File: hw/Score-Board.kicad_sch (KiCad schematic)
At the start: 95 parts, among them J1 Barrel_Jack, J2 Screw_Terminal_01x02, J3 Conn_01x04, J4 Conn_01x03, J5 Conn_01x04, J6 J-V3.3, J7 J-V12, J8 J-VSYS, Q1 2N3904, Q10 2N3905, Q11 2N3905, Q12 2N3905, Q13 2N3905, Q14 2N3905, Q15 2N3904, Q16 2N3904, Q17 2N3904, Q18 2N3904, Q19 2N3904, Q2 2N3904, Q20 2N3904, Q21 2N3904, Q22 2N3904, Q3 2N3904, Q4 2N3904, Q5 2N3904, Q6 2N3904, Q7 2N3904, Q8 2N3905, Q9 2N3905, SW1 RESET, SW2 NETWORK, U1 PicoW, U2 E18-MS1-PCB, U5 MCP1702-5002E

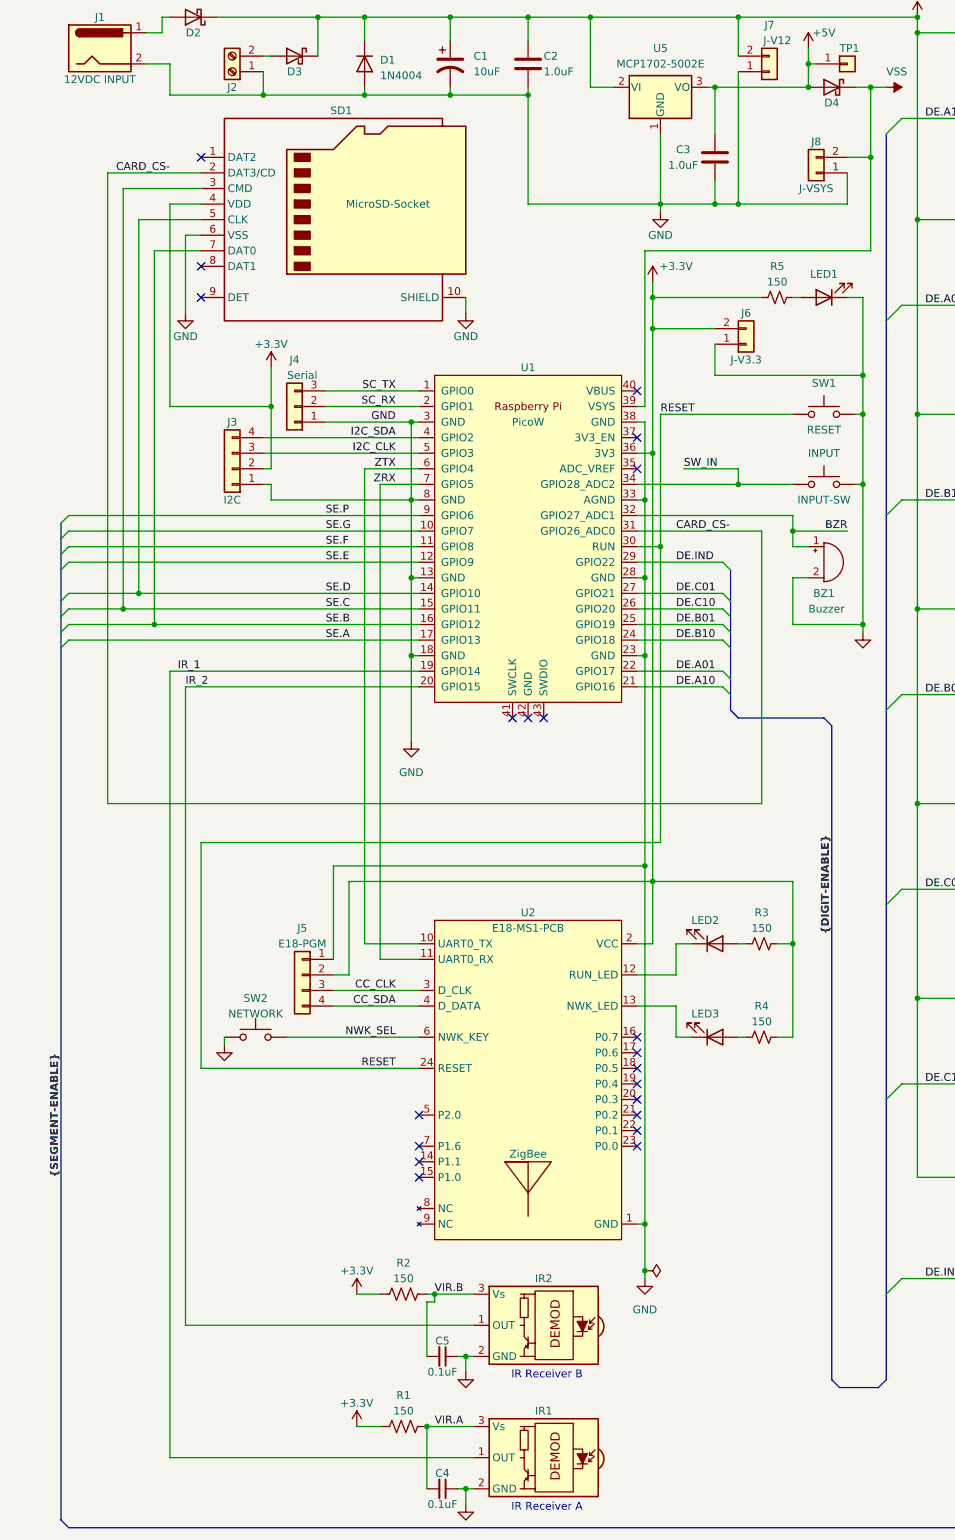
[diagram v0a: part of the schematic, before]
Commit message: SPI for display & SD, Seg&Dig enables 16 straight GPIOs.
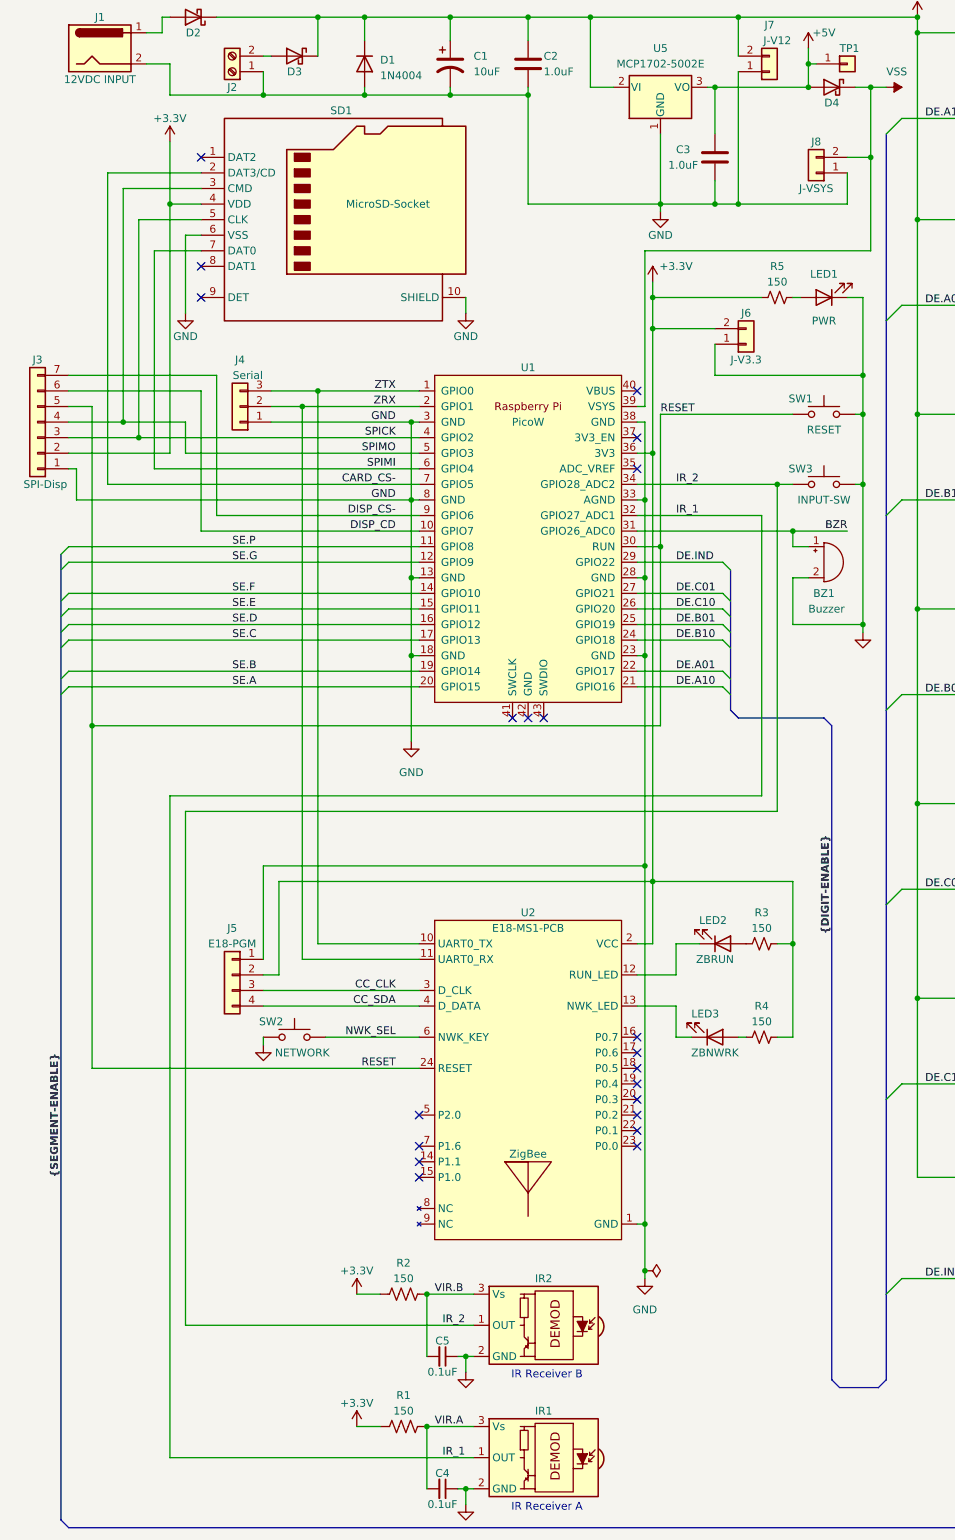
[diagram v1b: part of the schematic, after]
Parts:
- removed J3: Conn_01x04, Connector_PinHeader_2.54mm:PinHeader_1x04_P2.54mm_Vertical, symbol Connector_Generic:Conn_01x04
- added J3: SPI-Disp, Connector_PinSocket_2.54mm:PinSocket_1x07_P2.54mm_Vertical, symbol Connector_Generic:Conn_01x07
- C4, C5: footprint Capacitor_THT:CP_Radial_D5.0mm_P2.00mm -> Capacitor_THT:C_Disc_D5.0mm_W2.5mm_P2.50mm
- LED1: value LED -> PWR
- LED2: value LED -> ZBRUN
- LED3: value LED -> ZBNWRK
- renumbered INPUT to SW3
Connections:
- net SC_RX is gone; now on net ZRX: J4.2 (Pin_2), U1.2 (GPIO1)
- net SC_TX is gone; now on net ZTX: J4.3 (Pin_3), U1.1 (GPIO0)
- net SW_IN is gone; now on net IR_2: SW3.1, U1.34 (GPIO28_ADC2)
- net +3.3V: now also J3.2 (Pin_2)
- net BZR: now also U1.31 (GPIO26_ADC0); no longer U1.32 (GPIO27_ADC1)
- net CARD_CS-: now also U1.7 (GPIO5); no longer U1.31 (GPIO26_ADC0)
- net GND: now also J3.1 (Pin_1)
- net IR_1: now also U1.32 (GPIO27_ADC1); no longer U1.19 (GPIO14)
- net IR_2: no longer U1.20 (GPIO15)
- net RESET: now also J3.5 (Pin_5)
- net SE.A: now also U1.20 (GPIO15); no longer U1.17 (GPIO13)
- net SE.B: now also U1.19 (GPIO14); no longer SD1.7 (DAT0), U1.16 (GPIO12)
- net SE.C: now also U1.17 (GPIO13); no longer SD1.3 (CMD), U1.15 (GPIO11)
- net SE.D: now also U1.16 (GPIO12); no longer SD1.5 (CLK), U1.14 (GPIO10)
- net SE.E: now also U1.15 (GPIO11); no longer U1.12 (GPIO9)
- net SE.F: now also U1.14 (GPIO10); no longer U1.11 (GPIO8)
- net SE.G: now also U1.12 (GPIO9); no longer U1.10 (GPIO7)
- net SE.P: now also U1.11 (GPIO8); no longer U1.9 (GPIO6)
- net ZRX: no longer U1.7 (GPIO5)
- net ZTX: no longer U1.6 (GPIO4)
- net I2C_CLK renamed SPIMO
- net SPIMO: now also SD1.3 (CMD), J3.4 (Pin_4)
- net I2C_SDA renamed SPICK
- net SPICK: now also SD1.5 (CLK), J3.3 (Pin_3)
- new net DISP_CD: J3.6 (Pin_6), U1.10 (GPIO7)
- new net DISP_CS-: J3.7 (Pin_7), U1.9 (GPIO6)
- new net SPIMI: SD1.7 (DAT0), U1.6 (GPIO4)
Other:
- moved on the sheet: J4, J5, LED2, SW2

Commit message: Linear Style: Panel and Switches boards.
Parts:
- added C6: 10uf, symbol Device:C_Small
- added M1: MP1584EN, symbol AES_Library:AES-MP1584EN-DC_DC_CNV
- added R29: 4.7k, Resistor_THT:R_Axial_DIN0207_L6.3mm_D2.5mm_P10.16mm_Horizontal, symbol Device:R_Small_US
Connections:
- net +12V: now also M1.1 (Pos-In)
- net +3.3V: now also R29.1
- net +5V: now also M1.3 (Pos-Out)
- net GND: now also C6.2, M1.2 (Neg-In), M1.4 (Neg-Out)
- net RESET: now also C6.1, R29.2
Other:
- note added: "DC In (9V-24V) to 5V for Pico"
- moved on the sheet: C1, C2, D1, U5
